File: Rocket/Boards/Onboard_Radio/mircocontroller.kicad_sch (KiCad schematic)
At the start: 31 parts, among them J3 USB_B_Micro, J4 SWD JST PH, U4 STM32H562RGT6, Y2 12MHz

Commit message: updates
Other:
- note removed: "WTF IS THIS GOING TO GND????"

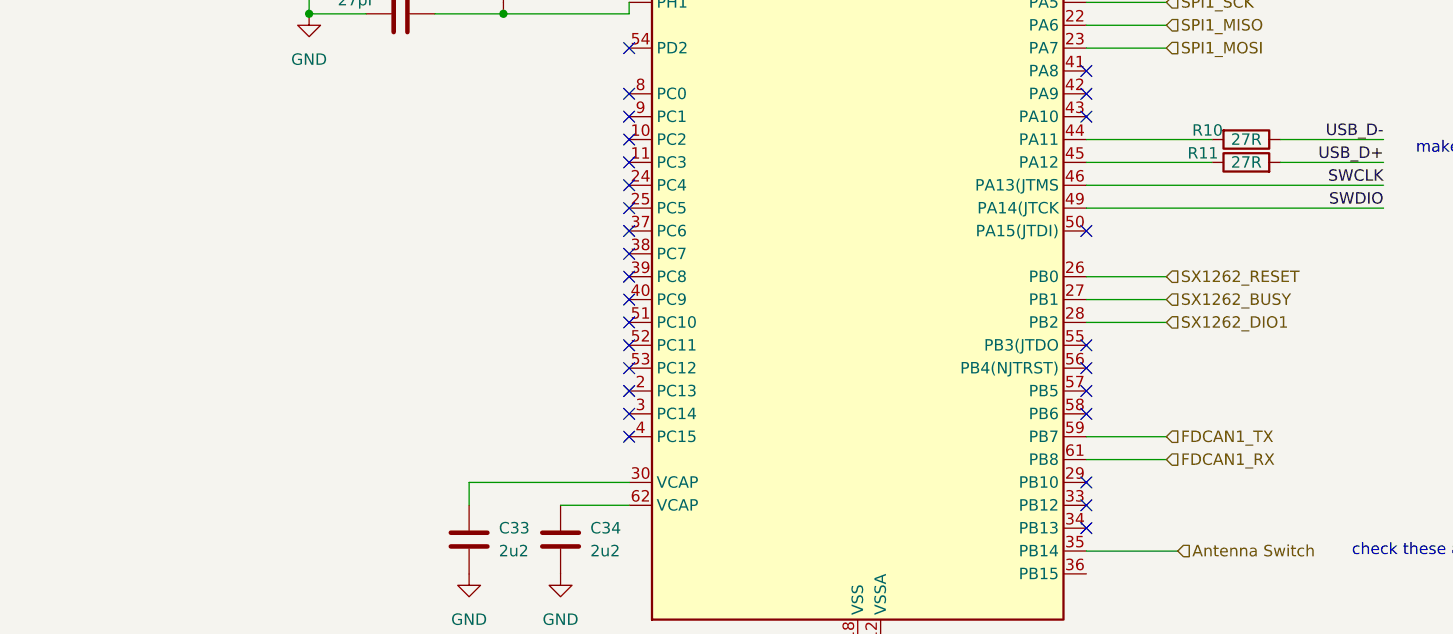
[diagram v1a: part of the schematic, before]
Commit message: can bus updeated
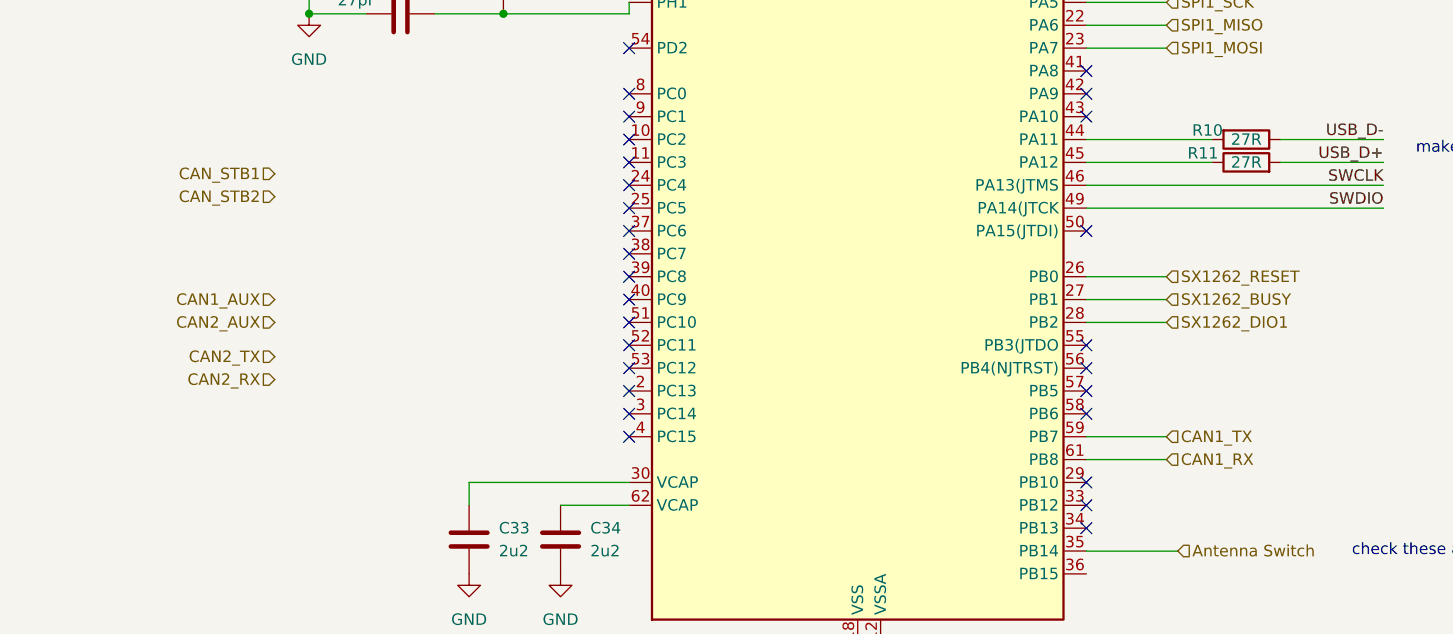
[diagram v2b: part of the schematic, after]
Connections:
- net FDCAN1_RX renamed CAN1_RX
- net FDCAN1_TX renamed CAN1_TX
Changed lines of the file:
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@@
 	(title_block
 		(title "Radio Microcontroller")
+		(date "2026-05-28")
 		(company "2026 Hybrid Rocket")
 		(comment 1 "Drawn by: Joella Tomkins")

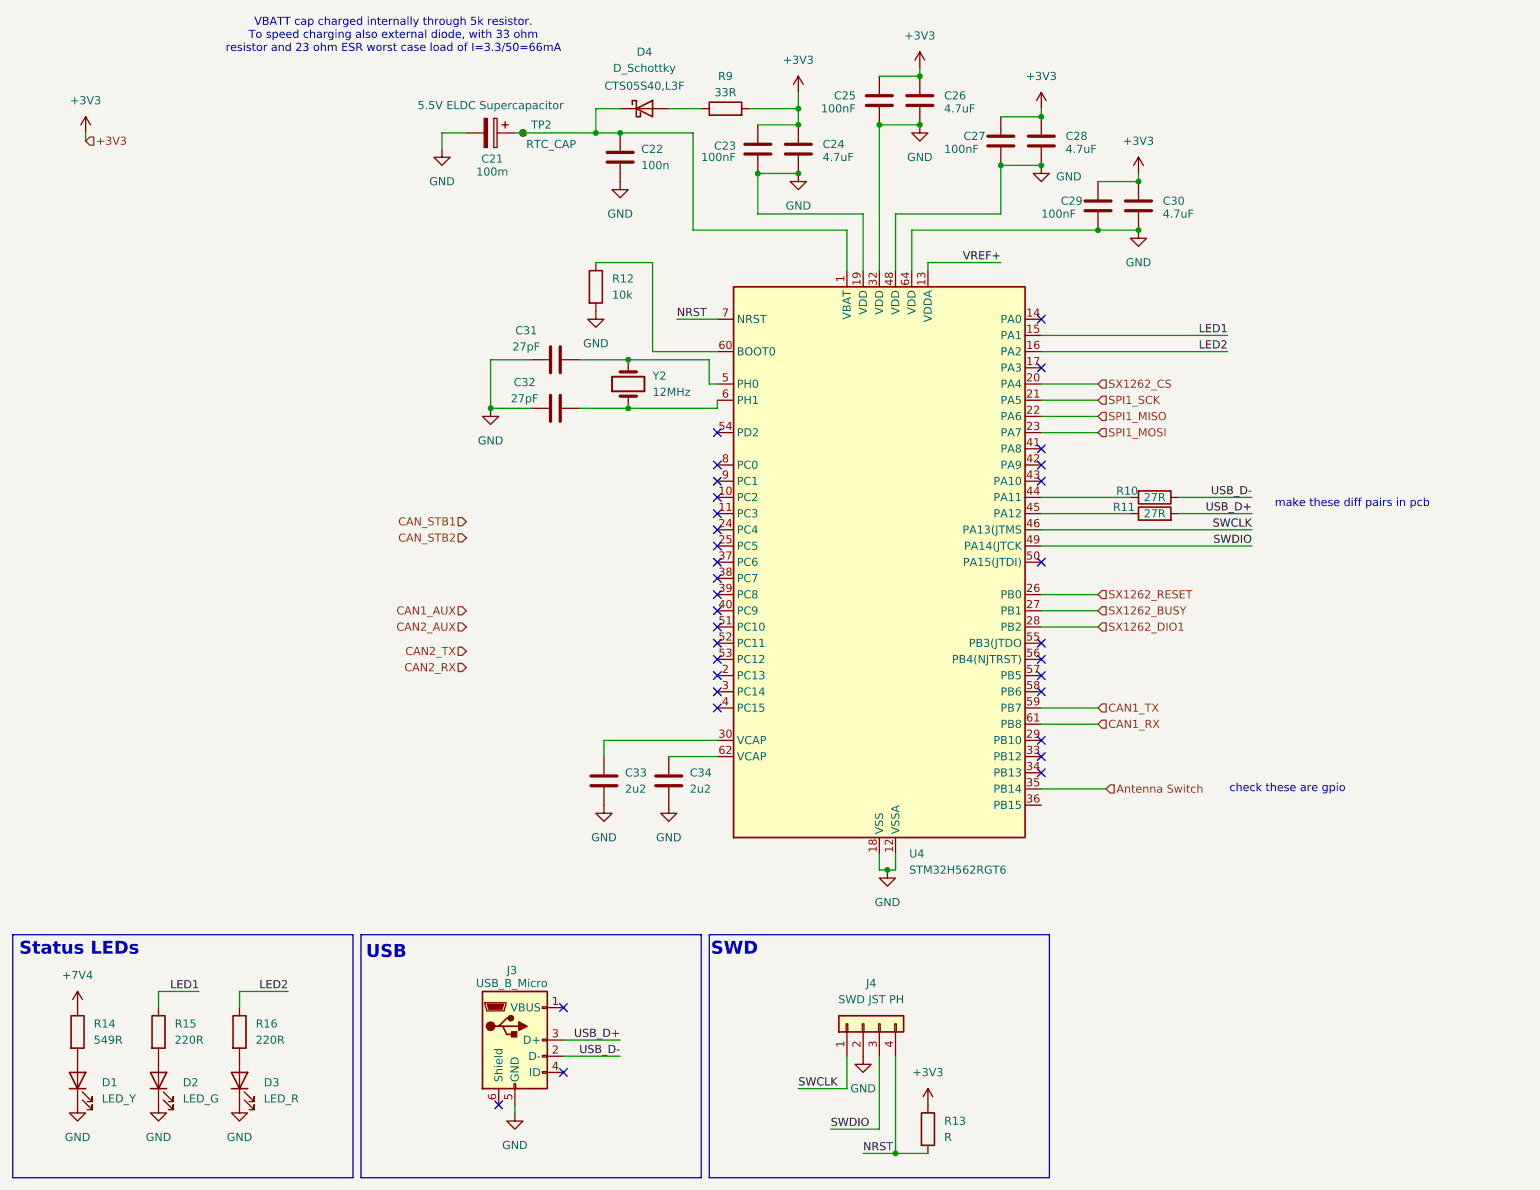
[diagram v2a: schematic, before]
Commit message: radio ic board planes joined, pcb made smaller, need to add cantraces before review
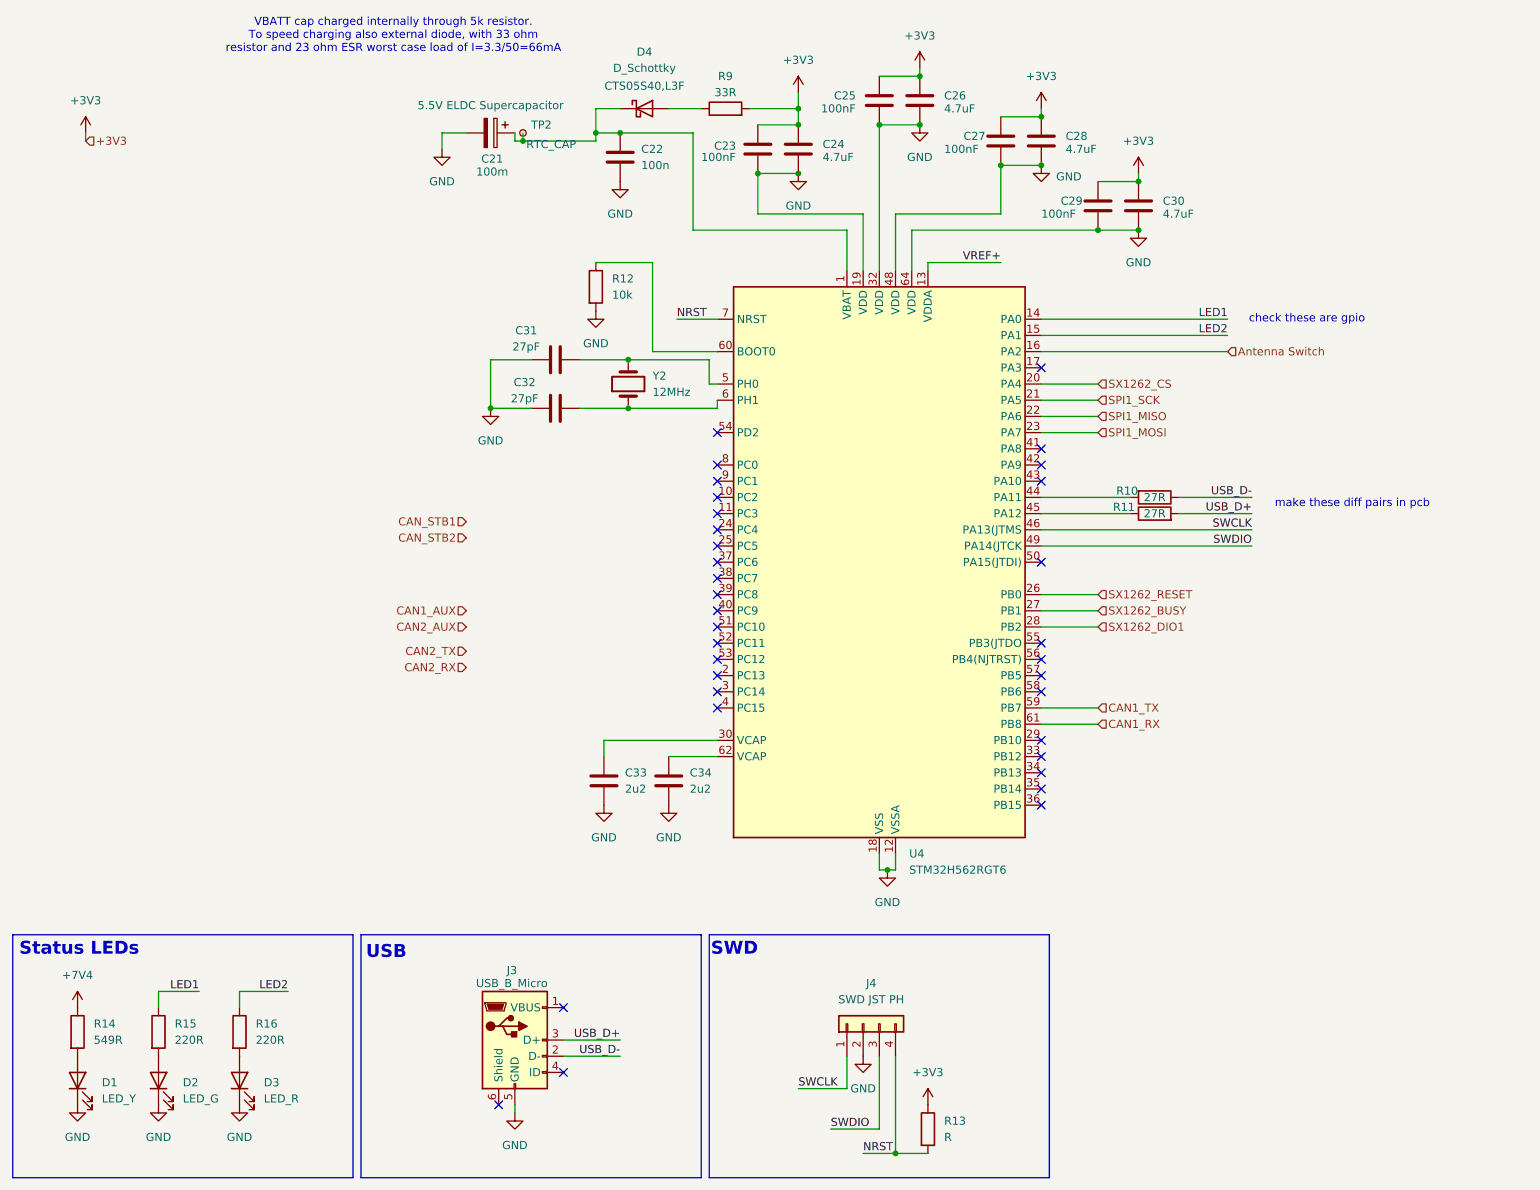
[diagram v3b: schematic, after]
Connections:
- net Antenna Switch: now also U4.16 (PA2); no longer U4.35 (PB14)
- net LED1: now also U4.14 (PA0); no longer U4.15 (PA1)
- net LED2: now also U4.15 (PA1); no longer U4.16 (PA2)
- no-connect marks 33 -> 34

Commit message: schematic ready for review
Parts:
- removed R13: R, Resistor_SMD:R_0603_1608Metric, symbol Device:R
- C22: MPN (none) -> KAM05FR71H104KH; Manufacturer (none) -> KYOCERA AVX; Voltage (none) -> 50V
- C33, C34: MPN (none) -> GRM188R61E225KA12D; Manufacturer (none) -> Murata Electronics; Voltage (none) -> 25V
- R12: MPN (none) -> RC0603FR-0710KL; Manufacturer (none) -> YAGEO
- R9: MPN (none) -> RC0201FR-0733RL; Manufacturer (none) -> YAGEO
- U4: MPN (none) -> STM32H562RGT6; Manufacturer (none) -> STMicroelectronics
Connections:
- net CAN1_AUX: now also U4.41 (PA8)
- net CAN2_AUX: now also U4.43 (PA10)
- net CAN_STB1: now also U4.42 (PA9)
- no-connect marks 34 -> 31

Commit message: updates
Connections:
- net MCU_D+: now reaches R11.1, U4.45 (PA12)
- net MCU_D-: now reaches R10.2, U4.44 (PA11)
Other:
- note removed: "make these diff pairs in pcb"
- moved on the sheet: R10, R11

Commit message: everything minus trace impedance and via stictching
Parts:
- renumbered D3 to D2, D2 to D3
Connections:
- net LED1: now also U4.52 (PC11); no longer U4.14 (PA0)
- net LED2: now also U4.51 (PC10); no longer U4.15 (PA1)
- net 3V3A_LDO_EN: now reaches U4.2 (PC13)
- net 3V3_LDO_EN: now reaches U4.3 (PC14)
- no-connect marks 31 -> 29
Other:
- note removed: "check these are gpio"
- moved on the sheet: R10, R11

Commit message: needs pcb and schematic review
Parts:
- C23, C25, C27, C29: LCSC Part # (none) -> C16194197
- C24, C26, C28, C30: LCSC Part # (none) -> C907917
- C31, C32: LCSC Part # (none) -> C909846
- C33, C34: LCSC Part # (none) -> C77047
- D1: LCSC Part # (none) -> C20433848
- D2: LCSC Part # (none) -> C23070302
- D3: LCSC Part # (none) -> C20433785
- D4: LCSC Part # (none) -> C396063
- J3: LCSC Part # (none) -> C132562
- J4: LCSC Part # (none) -> C131334
- R10, R11: LCSC Part # (none) -> C2484262
- R12: LCSC Part # (none) -> C98220
- R14: LCSC Part # (none) -> C4237517
- R15, R16: LCSC Part # (none) -> C2484076
- R9: LCSC Part # (none) -> C295794
- U4: LCSC Part # (none) -> C19711662

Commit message: updated swd and crystal
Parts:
- J4: footprint Connector_PinHeader_2.54mm:PinHeader_1x04_P2.54mm_Vertical -> Connector_JST:JST_PH_B4B-PH-K_1x04_P2.00mm_Vertical
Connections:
- net at C31.2, U4.5 (PH0): now also Y2.3 (2); no longer Y2.2
